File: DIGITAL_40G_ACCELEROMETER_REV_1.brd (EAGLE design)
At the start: 31.8 x 31.8 mm, 20 parts, among them IC1 ADIS16500AMLZ, IC2 LTC6820IUD#PBF, IC3 LDL1117S33R, T1 782482_33VC

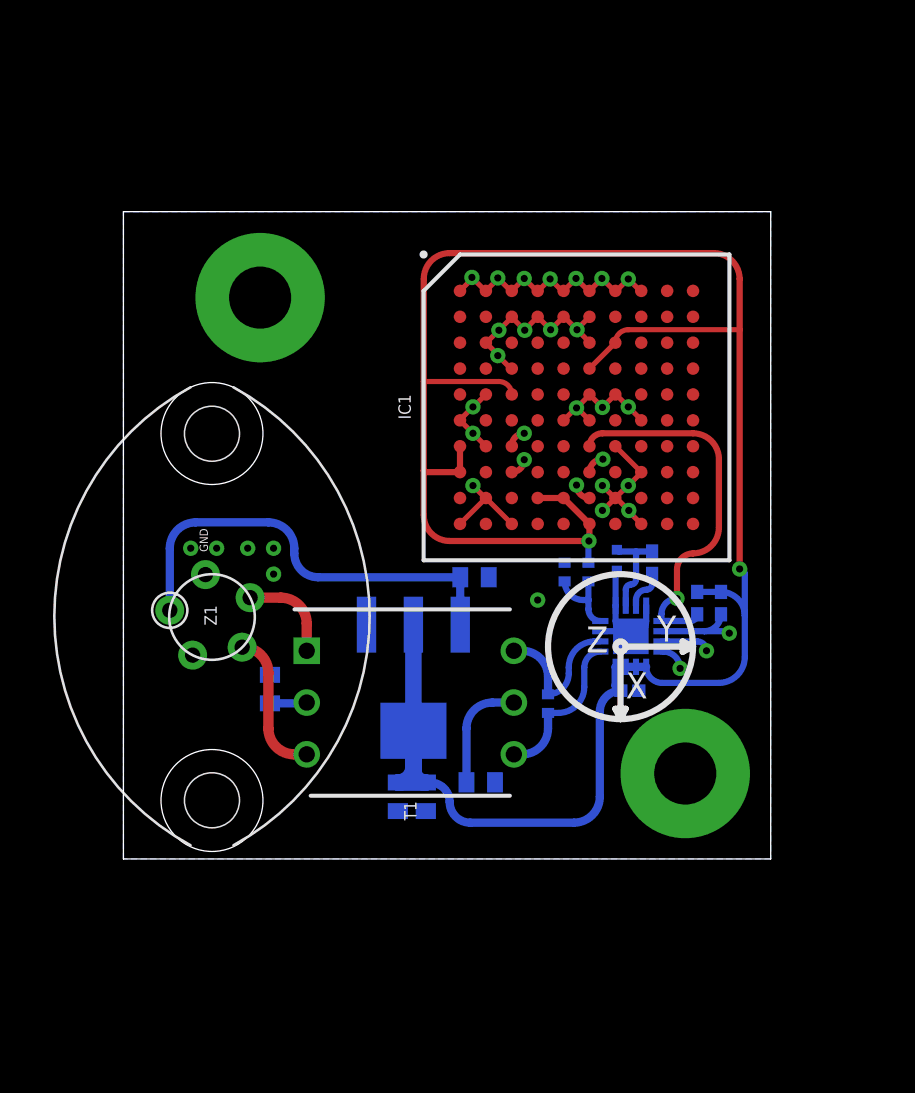
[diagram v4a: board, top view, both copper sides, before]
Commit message: Switched to 2 layer board
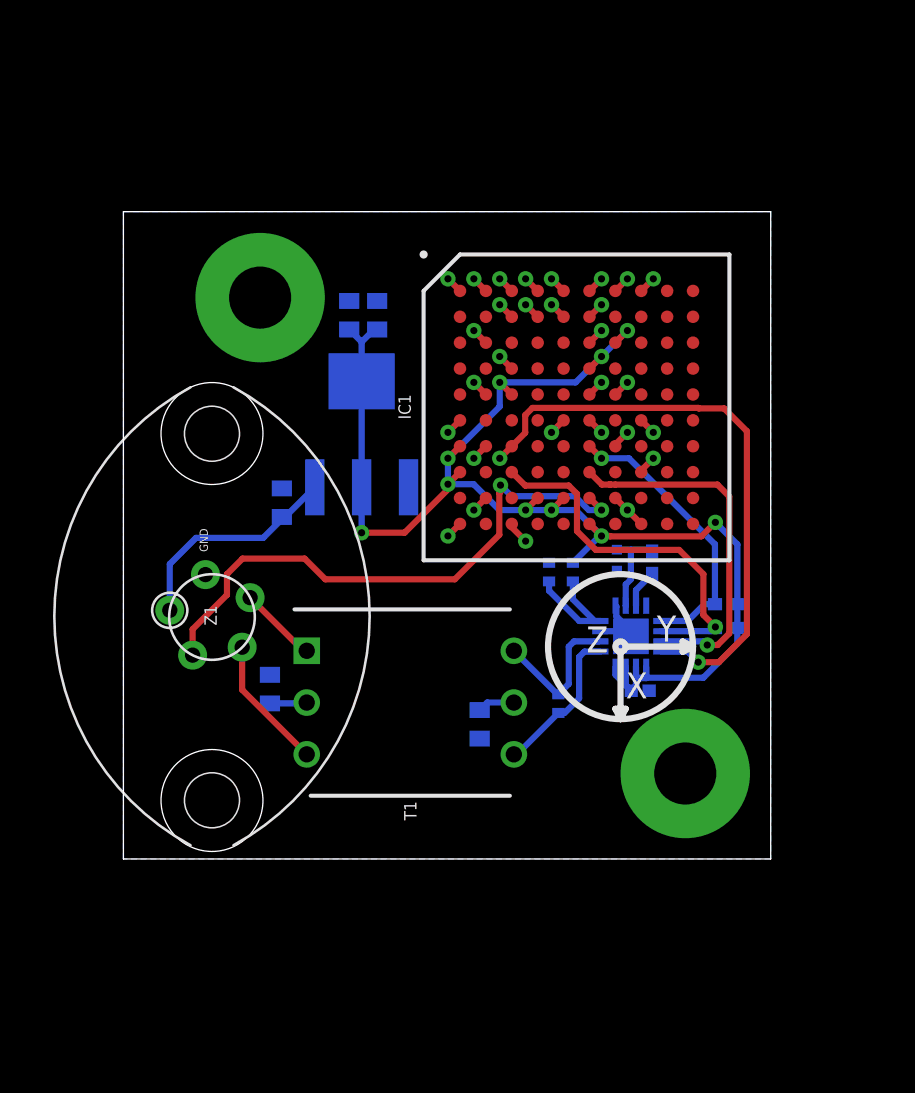
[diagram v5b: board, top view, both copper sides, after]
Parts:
- moved C3 23.9 mm to (11.1, 26.7), turned to 90 degrees
- moved C2 23.6 mm to (12.4, 26.7), turned to 90 degrees
- moved IC3 12.2 mm to (11.7, 20.8), turned to 90 degrees
- moved C1 10.1 mm to (7.77, 17.5), turned to 90 degrees
- moved C6 2.85 mm to (17.5, 6.60), turned to 270 degrees
- moved R12 1.42 mm to (29.6, 12.5), turned to 180 degrees
- moved R13 1.25 mm to (29.6, 11.3), turned to 180 degrees
- moved R16 0.76 mm to (20.9, 14.1)
- moved R17 0.76 mm to (22.0, 14.1)
- moved C4 0.51 mm to (25.3, 8.26)
- moved R11 0.51 mm to (21.3, 7.62)
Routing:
- net 3.3V: track 115.2 -> 70.3 mm, vias 2 -> 10
- net GND: track 50.9 -> 29.1 mm, vias 27 -> 29
- net 12V: track 21.4 -> 11.0 mm
- net CS: track 20.7 -> 29.1 mm, vias 3 -> 2
- net MOSI: track 18.1 -> 14.1 mm
- net MISO: track 21.8 -> 18.1 mm, vias 2 -> 1
- net N$1: track 5.49 -> 1.83 mm
- net DR: track 25.4 -> 28.4 mm, vias 1 -> 2
- net SLOW: track 3.73 -> 5.97 mm
- net SCK: track 16.3 -> 17.7 mm, vias 2 -> 1
- net IP: track 4.64 -> 3.86 mm
- removed copper zone on layer 15, net GND

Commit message: New layout. 2 layer board again. Updated 4PCB and regular version.
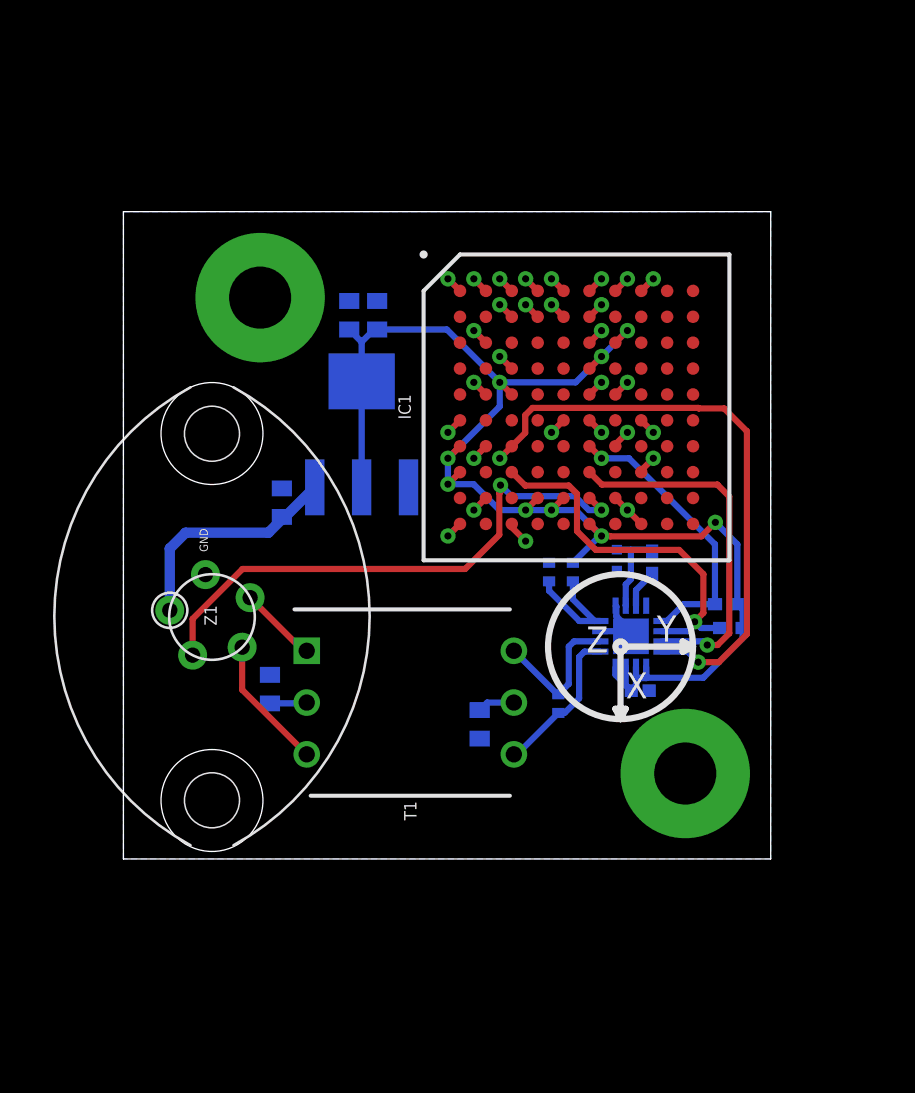
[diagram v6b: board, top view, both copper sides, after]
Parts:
- moved R13 0.25 mm to (29.8, 11.3)
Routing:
- net DR: track 28.4 -> 27.3 mm
- net 3.3V: track 70.3 -> 70.0 mm, vias 10 -> 9
